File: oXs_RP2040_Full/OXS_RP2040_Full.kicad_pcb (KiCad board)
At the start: 2 copper layers, 44.1 x 38.1 mm, 67 parts, among them J1 TLM/CRSF, J10 SPARE, J11 RMP, J2 V1/V2, J3 V3/V4, J4 GPS, J5 SELECT_POWER, J6 SBUS, J7 LIPO 8S, J8 MPU6050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

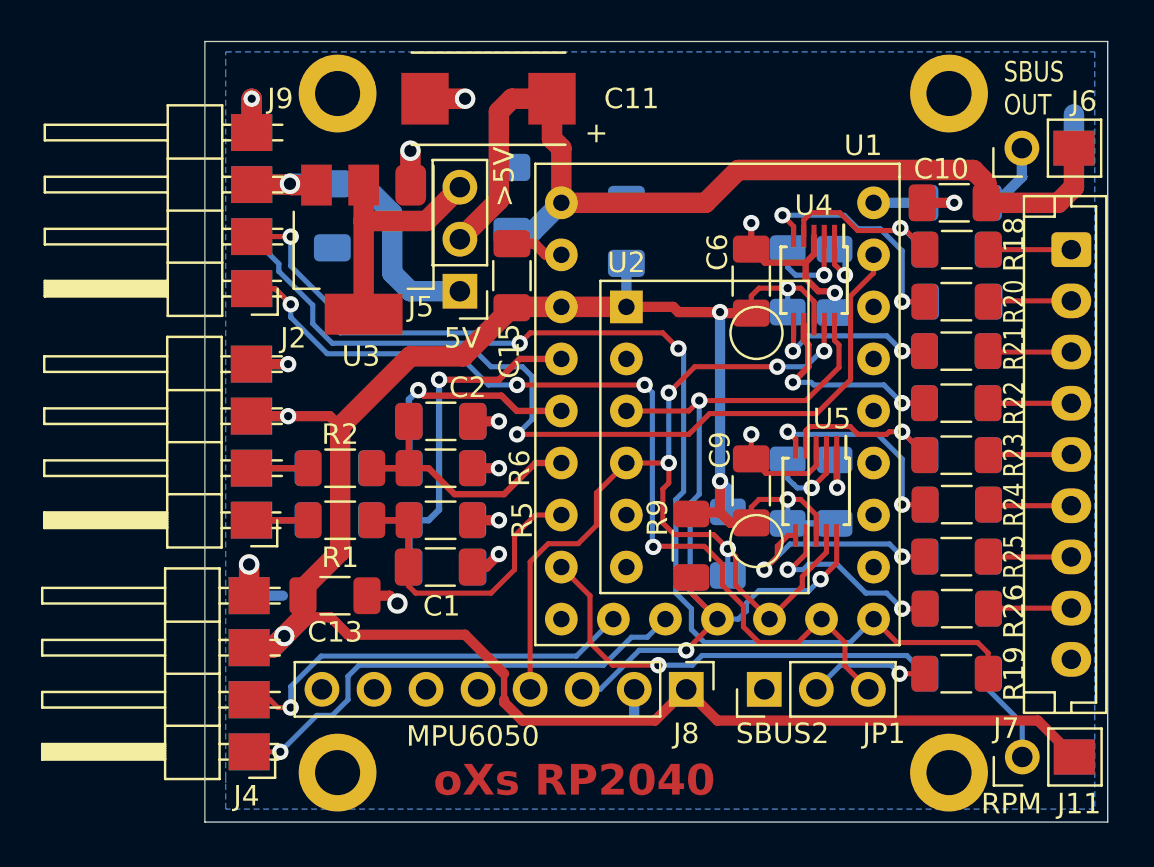
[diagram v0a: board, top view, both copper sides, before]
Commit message: replace mpu6050 connection
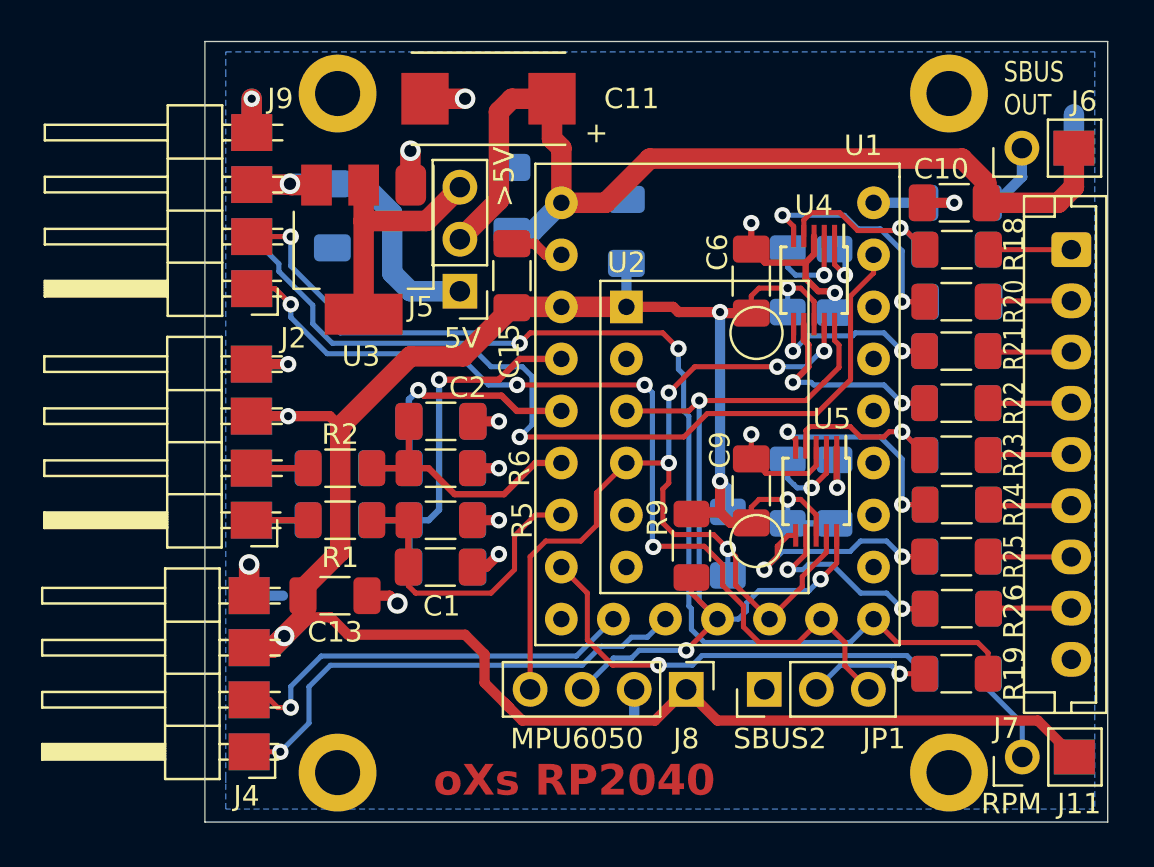
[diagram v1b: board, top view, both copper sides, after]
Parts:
- added REF**: WEEE-Logo_4.2x6mm_SilkScreen, Symbol:WEEE-Logo_4.2x6mm_SilkScreen, B.Cu at (80.5, 108.2)
- added REF**: OSHW-Logo2_7.3x6mm_SilkScreen, Symbol:OSHW-Logo2_7.3x6mm_SilkScreen, B.Cu at (88.3, 108.6)
- J8: footprint Connector_PinHeader_2.54mm:PinHeader_1x08_P2.54mm_Vertical -> Connector_PinHeader_2.54mm:PinHeader_1x04_P2.54mm_Vertical

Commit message: little adds
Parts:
- moved REF** 0.38 mm to (80.5, 108.6)
- moved REF** 0.25 mm to (88.3, 108.8)
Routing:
- net +3.3V: track 119.3 -> 118.3 mm

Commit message: update / build gerber
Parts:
- J7: value LIPO 8S -> 8 INPUT ALARMS
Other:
- board text added: "oXs RP2040 Full v1.0"
- board text removed: "oXs RP2040"
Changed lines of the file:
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@@
         (effects (font (size 1 1) (thickness 0.15)))
     )
-    (fp_text value "LIPO 8S" (at 9.144 0.127 90) (layer "F.Fab")
+    (fp_text value "8 INPUT ALARMS" (at 9.144 0.127 90) (layer "F.Fab")
         (effects (font (size 1 1) (thickness 0.15)))
     )
@@
     (property "ki_keywords" "cap capacitor")
     (attr smd)
-    (fp_text reference "C11" (at -6.985 0) (layer "F.SilkS")
+    (fp_text reference "C11" (at -5.842 -0.635) (layer "F.SilkS")
         (effects (font (size 1 1) (thickness 0.15)))
     )
@@
     )
   )
-  (footprint "Symbol:WEEE-Logo_4.2x6mm_SilkScreen" (layer "B.Cu")
+  (footprint "Symbol:WEEE-Logo_4.2x6mm_SilkScreen" locked (layer "B.Cu")
     (at 80.518 108.585 180)
     (descr "Waste Electrical and Electronic Equipment Directive")
@@
     )
   )
-  (footprint "Symbol:OSHW-Logo2_7.3x6mm_SilkScreen" (layer "B.Cu")
+  (footprint "Symbol:OSHW-Logo2_7.3x6mm_SilkScreen" locked (layer "B.Cu")
     (at 88.265 108.839 180)
     (descr "Open Source Hardware Symbol")
@@
   (gr_line (start 68.58 111.76) (end 112.649 111.76)
     (stroke (width 0.1) (type default)) (layer "F.Fab"))
-  (gr_text "oXs RP2040" (at 86.614 109.728) (layer "F.Cu")
+  (gr_text "oXs RP2040\nFull v1.0" (at 94.615 76.454) (layer "F.Cu")
     (effects (font (size 1.5 1.5) (thickness 0.31) bold))
   )
